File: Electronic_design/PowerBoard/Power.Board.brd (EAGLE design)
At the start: 100 x 80 mm, 33 parts, among them IC1 788TV, IC2 788TV

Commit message: ameliorations
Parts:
- U$1: value TROU_FIXATION -> (none)
- moved LED6 2.90 mm to (82.5, 6.22), turned to 270 degrees
- moved U$5 2.84 mm to (7.62, 74.9), turned to 0 degrees
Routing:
- net 12V: track 124.0 -> 78.3 mm
- net N$17: track 9.78 -> 9.02 mm
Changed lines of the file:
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@@
 <wire x1="0" y1="80" x2="0.381" y2="0" width="0" layer="20"/>
 <text x="5.08" y="2.54" size="1.778" layer="25" font="vector" rot="R90">LAAS_CNRS</text>
-<text x="15.24" y="73.66" size="1.778" layer="25" font="vector" rot="R180">GND</text>
+<text x="7.62" y="71.12" size="1.778" layer="25" font="vector" rot="R270">GND</text>
 <text x="88.9" y="66.04" size="1.778" layer="25" font="vector" rot="R270">GND</text>
 <text x="88.9" y="50.8" size="1.778" layer="25" font="vector">GND</text>
@@
 <text x="88.9" y="25.4" size="1.778" layer="25" font="vector">GND</text>
 <text x="93.98" y="2.54" size="1.778" layer="25" font="vector" rot="R180">GND</text>
-<text x="93.98" y="12.7" size="1.778" layer="25" font="vector" rot="R180">GND</text>
-<text x="10.16" y="63.5" size="1.778" layer="25" font="vector">12V</text>
+<text x="92.837" y="12.319" size="1.778" layer="25" font="vector" rot="R180">GND</text>
+<text x="16.51" y="71.12" size="1.778" layer="25" font="vector" rot="R270">12V</text>
 <text x="88.9" y="76.2" size="1.778" layer="25" font="vector" rot="R270">12V</text>
 <text x="88.9" y="55.88" size="1.778" layer="25" font="vector">12V</text>
@@
 <element name="MAST1" library="AUTO_FUSE" package="AUTO_FUSE" value="AUTO_FUSE" x="35.56" y="55.88"/>
 <element name="PAP1" library="AUTO_FUSE" package="AUTO_FUSE" value="AUTO_FUSE" x="35.56" y="43.18"/>
-<element name="U$5" library="PowerHeaders" package="3MM_HEADER_2" value="3MM_HEADER_2" x="5.08" y="73.66" rot="R270"/>
+<element name="U$5" library="PowerHeaders" package="3MM_HEADER_2" value="3MM_HEADER_2" x="7.62" y="74.93"/>
 <element name="0D2" library="AUTO_FUSE" package="AUTO_FUSE" value="AUTO_FUSE" x="58.42" y="68.58"/>
 <element name="MAST2" library="AUTO_FUSE" package="AUTO_FUSE" value="AUTO_FUSE" x="58.42" y="55.88"/>
@@
 <attribute name="SPICEPREFIX" value="R" x="78.74" y="7.62" size="1.778" layer="27" rot="R90" display="off"/>
 </element>
-<element name="LED6" library="eagle-ltspice" library_urn="urn:adsk.eagle:library:217" package="LED_LD260" package3d_urn="urn:adsk.eagle:package:13313/1" value="" x="85.217" y="5.08">
-<attribute name="SPICEMODEL" value="NONE" x="85.217" y="5.08" size="1.778" layer="27" display="off"/>
-<attribute name="SPICEPREFIX" value="D" x="85.217" y="5.08" size="1.778" layer="27" display="off"/>
-<attribute name="SPICETYPE" value="diode" x="85.217" y="5.08" size="1.778" layer="27" display="off"/>
+<element name="LED6" library="eagle-ltspice" library_urn="urn:adsk.eagle:library:217" package="LED_LD260" package3d_urn="urn:adsk.eagle:package:13313/1" value="" x="82.55" y="6.223" rot="R270">
+<attribute name="SPICEMODEL" value="NONE" x="82.55" y="6.223" size="1.778" layer="27" rot="R270" display="off"/>
+<attribute name="SPICEPREFIX" value="D" x="82.55" y="6.223" size="1.778" layer="27" rot="R270" display="off"/>
+<attribute name="SPICETYPE" value="diode" x="82.55" y="6.223" size="1.778" layer="27" rot="R270" display="off"/>
 </element>
 <element name="IC2" library="linear" library_urn="urn:adsk.eagle:library:262" package="TO220V" package3d_urn="urn:adsk.eagle:package:16417/1" value="788TV" x="58.42" y="7.62"/>
-<element name="U$1" library="Trous_fixation" package="TROUS_FIXATION" value="TROU_FIXATION" x="0" y="0"/>
+<element name="U$1" library="Trous_fixation" package="TROUS_FIXATION" value="" x="0" y="0"/>
 </elements>
 <signals>
@@
 <contactref element="RPI" pad="1A"/>
 <contactref element="FNU1" pad="P$2"/>
-<wire x1="22.86" y1="63.5" x2="5.08" y2="63.5" width="5" layer="16"/>
-<wire x1="22.86" y1="63.5" x2="24.13" y2="63.5" width="5" layer="16"/>
-<wire x1="24.13" y1="63.5" x2="28.45" y2="67.82" width="5" layer="16"/>
-<wire x1="28.45" y1="67.82" x2="28.45" y2="68.58" width="5" layer="16"/>
-<wire x1="28.45" y1="57.91" x2="28.45" y2="55.88" width="5" layer="16"/>
-<wire x1="28.45" y1="57.91" x2="22.86" y2="63.5" width="5" layer="16"/>
-<wire x1="28.45" y1="67.82" x2="28.45" y2="68.58" width="5" layer="1"/>
-<wire x1="22.86" y1="63.5" x2="24.13" y2="63.5" width="5" layer="1"/>
-<wire x1="24.13" y1="63.5" x2="28.45" y2="67.82" width="5" layer="1"/>
-<wire x1="28.45" y1="57.91" x2="28.45" y2="55.88" width="5" layer="1"/>
-<wire x1="28.45" y1="57.91" x2="22.86" y2="63.5" width="5" layer="1"/>
 <wire x1="28.45" y1="55.88" x2="28.45" y2="43.18" width="5" layer="1"/>
 <wire x1="28.45" y1="43.18" x2="28.45" y2="30.48" width="5" layer="1"/>
@@
 <wire x1="25.146" y1="15.24" x2="25.146" y2="5.334" width="5" layer="1"/>
 <wire x1="25.146" y1="5.334" x2="25.4" y2="5.08" width="5" layer="1"/>
-<wire x1="5.08" y1="63.5" x2="22.86" y2="63.5" width="5" layer="1"/>
+<wire x1="28.45" y1="68.58" x2="28.45" y2="55.88" width="5" layer="1"/>
+<wire x1="17.78" y1="74.93" x2="24.13" y2="68.58" width="6" layer="1"/>
+<wire x1="24.13" y1="68.58" x2="28.45" y2="68.58" width="6" layer="1"/>
 </signal>
 <signal name="N$2">
@@
 <contactref element="R6" pad="1"/>
 <contactref element="IC2" pad="3"/>
-<wire x1="60.96" y1="5.08" x2="68.58" y2="5.08" width="2.54" layer="16"/>
-<wire x1="68.58" y1="5.08" x2="71.12" y2="2.54" width="2.54" layer="16"/>
-<wire x1="71.12" y1="2.54" x2="78.74" y2="2.54" width="2.54" layer="16"/>
-<wire x1="78.74" y1="2.54" x2="88.9" y2="2.54" width="2.54" layer="16"/>
-<wire x1="88.9" y1="2.54" x2="91.44" y2="5.08" width="2.54" layer="16"/>
-<wire x1="91.44" y1="5.08" x2="96.52" y2="5.08" width="2.54" layer="16"/>
+<wire x1="60.96" y1="5.08" x2="67.31" y2="5.08" width="1.27" layer="16"/>
+<wire x1="67.31" y1="5.08" x2="69.85" y2="2.54" width="1.27" layer="16"/>
+<wire x1="69.85" y1="2.54" x2="78.74" y2="2.54" width="1.27" layer="16"/>
+<wire x1="78.74" y1="2.54" x2="88.9" y2="2.54" width="1.27" layer="16"/>
+<wire x1="88.9" y1="2.54" x2="91.44" y2="5.08" width="1.27" layer="16"/>
+<wire x1="91.44" y1="5.08" x2="96.52" y2="5.08" width="1.27" layer="16"/>
 </signal>
 <signal name="N$5">
@@
 <contactref element="R6" pad="2"/>
 <contactref element="LED6" pad="A"/>
-<wire x1="78.74" y1="12.7" x2="83.947" y2="7.493" width="1.27" layer="16"/>
-<wire x1="83.947" y1="7.493" x2="83.947" y2="5.08" width="1.27" layer="16"/>
+<wire x1="78.74" y1="12.7" x2="82.55" y2="12.7" width="1.27" layer="16"/>
+<wire x1="82.55" y1="12.7" x2="82.55" y2="7.493" width="1.27" layer="16"/>
 </signal>
 <signal name="N$18">

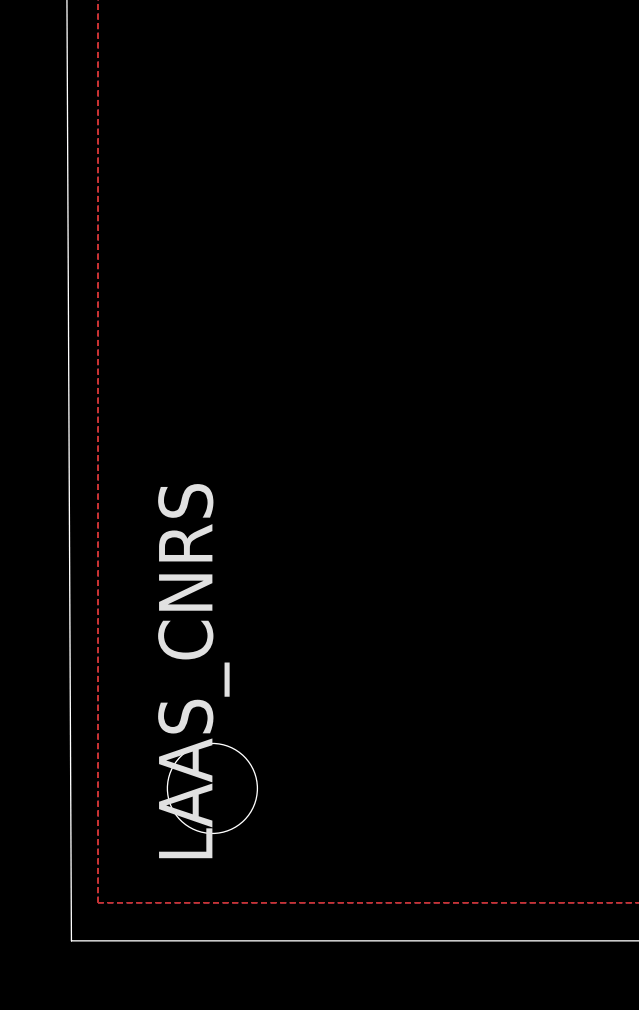
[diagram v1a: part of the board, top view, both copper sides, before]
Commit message: elargissement pistes
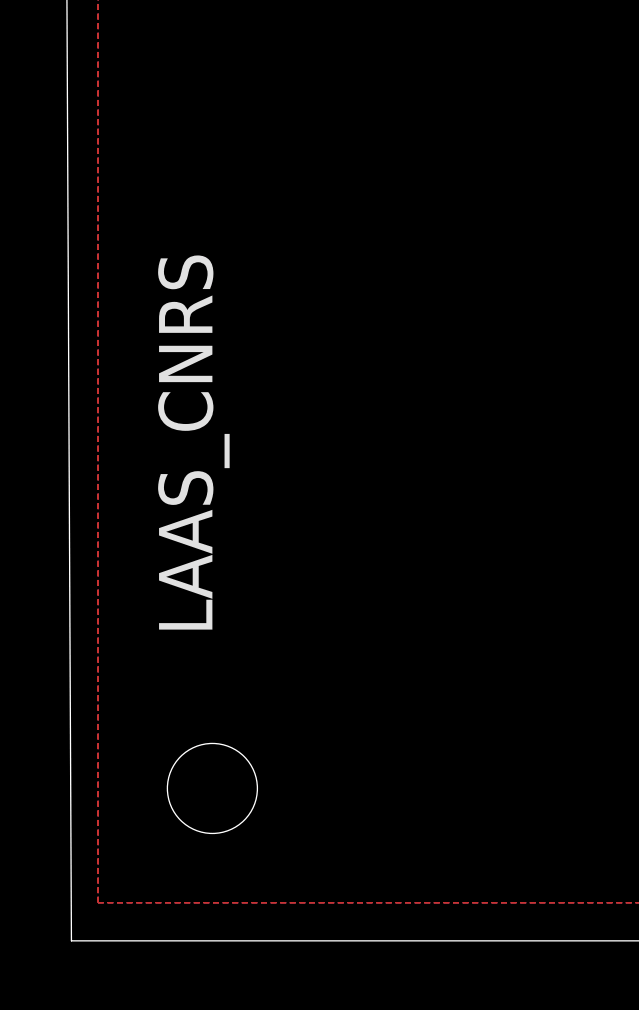
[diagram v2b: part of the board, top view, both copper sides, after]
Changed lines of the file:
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@@
 <wire x1="100" y1="80" x2="0" y2="80" width="0" layer="20"/>
 <wire x1="0" y1="80" x2="0.381" y2="0" width="0" layer="20"/>
-<text x="5.08" y="2.54" size="1.778" layer="25" font="vector" rot="R90">LAAS_CNRS</text>
+<text x="5.08" y="10.16" size="1.778" layer="25" font="vector" rot="R90">LAAS_CNRS</text>
 <text x="7.62" y="71.12" size="1.778" layer="25" font="vector" rot="R270">GND</text>
 <text x="88.9" y="66.04" size="1.778" layer="25" font="vector" rot="R270">GND</text>

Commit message: modif plan de masse
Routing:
- net 12V: track 78.3 -> 0.00 mm
- net N$6: track 36.9 -> 6.34 mm
- added copper zone on layer 1, net 12V
- added copper zone on layer 1, net N$6
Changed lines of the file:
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@@
 <contactref element="RPI" pad="1A"/>
 <contactref element="FNU1" pad="P$2"/>
-<wire x1="28.45" y1="55.88" x2="28.45" y2="43.18" width="5" layer="1"/>
-<wire x1="28.45" y1="43.18" x2="28.45" y2="30.48" width="5" layer="1"/>
-<wire x1="28.45" y1="30.48" x2="28.45" y2="25.91" width="5" layer="1"/>
-<wire x1="28.45" y1="25.91" x2="25.4" y2="22.86" width="5" layer="1"/>
-<wire x1="25.4" y1="22.86" x2="25.4" y2="15.494" width="5" layer="1"/>
-<wire x1="25.4" y1="15.494" x2="25.146" y2="15.24" width="5" layer="1"/>
-<wire x1="25.146" y1="15.24" x2="25.146" y2="5.334" width="5" layer="1"/>
-<wire x1="25.146" y1="5.334" x2="25.4" y2="5.08" width="5" layer="1"/>
-<wire x1="28.45" y1="68.58" x2="28.45" y2="55.88" width="5" layer="1"/>
-<wire x1="17.78" y1="74.93" x2="24.13" y2="68.58" width="6" layer="1"/>
-<wire x1="24.13" y1="68.58" x2="28.45" y2="68.58" width="6" layer="1"/>
+<polygon width="0.508" layer="1">
+<vertex x="1.27" y="78.74"/>
+<vertex x="35.56" y="78.74"/>
+<vertex x="35.60955" y="1.2763125"/>
+<vertex x="1.195678125" y="1.20198125"/>
+</polygon>
 </signal>
 <signal name="N$2">
@@
 <wire x1="65.53" y1="68.58" x2="68.58" y2="65.53" width="1.27" layer="16"/>
 <wire x1="68.58" y1="65.53" x2="68.58" y2="63.5" width="1.27" layer="16"/>
-<wire x1="65.53" y1="68.58" x2="68.58" y2="68.58" width="5" layer="1"/>
-<wire x1="68.58" y1="68.58" x2="73.66" y2="73.66" width="5" layer="1"/>
-<wire x1="73.66" y1="73.66" x2="93.98" y2="73.66" width="5" layer="1"/>
+<polygon width="0.508" layer="1">
+<vertex x="58.42" y="78.74"/>
+<vertex x="99.06" y="78.74"/>
+<vertex x="99.06" y="68.58"/>
+<vertex x="88.9" y="68.58"/>
+<vertex x="88.9" y="64.77"/>
+<vertex x="58.42" y="64.77"/>
+</polygon>
 </signal>
 <signal name="N$7">
@@
 <contactref element="MAST2" pad="P$4"/>
 <contactref element="R2" pad="1"/>
-<wire x1="65.53" y1="55.88" x2="76.2" y2="55.88" width="2.54" layer="16"/>
-<wire x1="76.2" y1="55.88" x2="95.25" y2="55.88" width="2.54" layer="16"/>
+<wire x1="65.53" y1="55.88" x2="76.2" y2="55.88" width="3" layer="16"/>
+<wire x1="76.2" y1="55.88" x2="95.25" y2="55.88" width="3" layer="16"/>
 </signal>
 <signal name="GND">
@@
 <contactref element="LED6" pad="K"/>
 <contactref element="IC2" pad="2"/>
-<polygon width="0.508" layer="1">
+<polygon width="0.508" layer="16">
 <vertex x="1.27" y="78.74"/>
 <vertex x="99.06" y="78.74"/>
@@
 </polygon>
 <polygon width="0.508" layer="1">
-<vertex x="1.27" y="78.74"/>
-<vertex x="99.06" y="78.74"/>
+<vertex x="36.83" y="78.74"/>
+<vertex x="57.15" y="78.74"/>
+<vertex x="57.15" y="63.5"/>
+<vertex x="90.17" y="63.5"/>
+<vertex x="90.17" y="67.31"/>
+<vertex x="99.06" y="67.31"/>
 <vertex x="99.06" y="1.27"/>
-<vertex x="1.27" y="1.27"/>
-</polygon>
-<polygon width="0.508" layer="16">
-<vertex x="1.27" y="78.74"/>
-<vertex x="99.06" y="78.74"/>
-<vertex x="99.06" y="1.27"/>
-<vertex x="1.27" y="1.27"/>
+<vertex x="36.83" y="1.27"/>
 </polygon>
 </signal>
@@
 <contactref element="PAP" pad="P$1"/>
 <contactref element="R3" pad="1"/>
-<wire x1="65.53" y1="43.18" x2="73.66" y2="43.18" width="2.54" layer="16"/>
-<wire x1="73.66" y1="43.18" x2="95.25" y2="43.18" width="2.54" layer="16"/>
+<wire x1="65.53" y1="43.18" x2="73.66" y2="43.18" width="3" layer="16"/>
+<wire x1="73.66" y1="43.18" x2="95.25" y2="43.18" width="3" layer="16"/>
 </signal>
 <signal name="N$8">

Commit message: ajout condensateurs
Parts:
- added C1, C2, C3: (no value), rcl:E7,5-18
- added C4: (no value), rcl:E5-13
- moved LED1 12.7 mm to (82.5, 76.2)
- moved R1 12.7 mm to (73.7, 76.2)
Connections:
- net 12V: now also C1.+, C2.+, C3.+
- net GND: now also C1.-, C2.-, C3.-, C4.-
- net N$6: now also C4.+
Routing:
- net N$6: track 6.34 -> 0.00 mm
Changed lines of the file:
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@@
 <wire x1="100" y1="80" x2="0" y2="80" width="0" layer="20"/>
 <wire x1="0" y1="80" x2="0.381" y2="0" width="0" layer="20"/>
-<text x="5.08" y="10.16" size="1.778" layer="25" font="vector" rot="R90">LAAS_CNRS</text>
+<text x="20.32" y="6.35" size="1.778" layer="25" font="vector" rot="R180">LAAS_CNRS</text>
 <text x="7.62" y="71.12" size="1.778" layer="25" font="vector" rot="R270">GND</text>
 <text x="88.9" y="66.04" size="1.778" layer="25" font="vector" rot="R270">GND</text>
@@
 <element name="FNU2" library="AUTO_FUSE" package="AUTO_FUSE" value="AUTO_FUSE" x="58.42" y="30.48"/>
 <element name="NOTUSE" library="PowerHeaders" package="GREEN_HEADER" value="GREEN_HEADER" x="95.25" y="27.94" rot="R270"/>
-<element name="LED1" library="eagle-ltspice" library_urn="urn:adsk.eagle:library:217" package="LED_LD260" package3d_urn="urn:adsk.eagle:package:13313/1" value="" x="82.55" y="63.5">
-<attribute name="SPICEMODEL" value="NONE" x="82.55" y="63.5" size="1.778" layer="27" display="off"/>
-<attribute name="SPICEPREFIX" value="D" x="82.55" y="63.5" size="1.778" layer="27" display="off"/>
-<attribute name="SPICETYPE" value="diode" x="82.55" y="63.5" size="1.778" layer="27" display="off"/>
-</element>
-<element name="R1" library="eagle-ltspice" library_urn="urn:adsk.eagle:library:217" package="0207/10" package3d_urn="urn:adsk.eagle:package:13275/1" value="" x="73.66" y="63.5">
-<attribute name="SPICEMODEL" value="NONE" x="73.66" y="63.5" size="1.778" layer="27" display="off"/>
-<attribute name="SPICEPREFIX" value="R" x="73.66" y="63.5" size="1.778" layer="27" display="off"/>
+<element name="LED1" library="eagle-ltspice" library_urn="urn:adsk.eagle:library:217" package="LED_LD260" package3d_urn="urn:adsk.eagle:package:13313/1" value="" x="82.55" y="76.2">
+<attribute name="SPICEMODEL" value="NONE" x="82.55" y="76.2" size="1.778" layer="27" display="off"/>
+<attribute name="SPICEPREFIX" value="D" x="82.55" y="76.2" size="1.778" layer="27" display="off"/>
+<attribute name="SPICETYPE" value="diode" x="82.55" y="76.2" size="1.778" layer="27" display="off"/>
+</element>
+<element name="R1" library="eagle-ltspice" library_urn="urn:adsk.eagle:library:217" package="0207/10" package3d_urn="urn:adsk.eagle:package:13275/1" value="" x="73.66" y="76.2">
+<attribute name="SPICEMODEL" value="NONE" x="73.66" y="76.2" size="1.778" layer="27" display="off"/>
+<attribute name="SPICEPREFIX" value="R" x="73.66" y="76.2" size="1.778" layer="27" display="off"/>
 </element>
 <element name="R2" library="eagle-ltspice" library_urn="urn:adsk.eagle:library:217" package="0207/10" package3d_urn="urn:adsk.eagle:package:13275/1" value="" x="76.2" y="50.8" rot="R270">
@@
 <element name="IC2" library="linear" library_urn="urn:adsk.eagle:library:262" package="TO220V" package3d_urn="urn:adsk.eagle:package:16417/1" value="788TV" x="58.42" y="7.62"/>
 <element name="U$1" library="Trous_fixation" package="TROUS_FIXATION" value="" x="0" y="0"/>
+<element name="C1" library="rcl" library_urn="urn:adsk.eagle:library:334" package="E7,5-18" package3d_urn="urn:adsk.eagle:package:23379/1" value="" x="13.97" y="57.15"/>
+<element name="C2" library="rcl" library_urn="urn:adsk.eagle:library:334" package="E7,5-18" package3d_urn="urn:adsk.eagle:package:23379/1" value="" x="13.97" y="39.37"/>
+<element name="C3" library="rcl" library_urn="urn:adsk.eagle:library:334" package="E7,5-18" package3d_urn="urn:adsk.eagle:package:23379/1" value="" x="13.97" y="21.59"/>
+<element name="C4" library="rcl" library_urn="urn:adsk.eagle:library:334" package="E5-13" package3d_urn="urn:adsk.eagle:package:23375/1" value="" x="76.2" y="64.77" rot="R270"/>
 </elements>
 <signals>
@@
 <vertex x="1.195678125" y="1.20198125"/>
 </polygon>
+<contactref element="C1" pad="+"/>
+<contactref element="C2" pad="+"/>
+<contactref element="C3" pad="+"/>
 </signal>
 <signal name="N$2">
@@
 <contactref element="OD" pad="P$1"/>
 <contactref element="R1" pad="1"/>
-<wire x1="65.53" y1="68.58" x2="68.58" y2="65.53" width="1.27" layer="16"/>
-<wire x1="68.58" y1="65.53" x2="68.58" y2="63.5" width="1.27" layer="16"/>
 <polygon width="0.508" layer="1">
 <vertex x="58.42" y="78.74"/>
@@
 <vertex x="58.42" y="64.77"/>
 </polygon>
+<contactref element="C4" pad="+"/>
 </signal>
 <signal name="N$7">
@@
 <vertex x="36.83" y="1.27"/>
 </polygon>
+<contactref element="C1" pad="-"/>
+<contactref element="C2" pad="-"/>
+<contactref element="C3" pad="-"/>
+<contactref element="C4" pad="-"/>
 </signal>
 <signal name="N$1">
@@
 <contactref element="LED1" pad="A"/>
 <contactref element="R1" pad="2"/>
-<wire x1="78.74" y1="63.5" x2="81.28" y2="63.5" width="1.27" layer="16"/>
+<wire x1="78.74" y1="76.2" x2="81.28" y2="76.2" width="1.27" layer="16"/>
 </signal>
 <signal name="N$13">

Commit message: modif sens connecteurs puissance
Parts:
- moved U$5 10.2 mm to (17.8, 74.9), turned to 180 degrees
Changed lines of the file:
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@@
 <wire x1="0" y1="80" x2="0.381" y2="0" width="0" layer="20"/>
 <text x="20.32" y="6.35" size="1.778" layer="25" font="vector" rot="R180">LAAS_CNRS</text>
-<text x="7.62" y="71.12" size="1.778" layer="25" font="vector" rot="R270">GND</text>
+<text x="16.51" y="71.12" size="1.778" layer="25" font="vector" rot="R270">GND</text>
 <text x="88.9" y="66.04" size="1.778" layer="25" font="vector" rot="R270">GND</text>
 <text x="88.9" y="50.8" size="1.778" layer="25" font="vector">GND</text>
@@
 <text x="93.98" y="2.54" size="1.778" layer="25" font="vector" rot="R180">GND</text>
 <text x="92.837" y="12.319" size="1.778" layer="25" font="vector" rot="R180">GND</text>
-<text x="16.51" y="71.12" size="1.778" layer="25" font="vector" rot="R270">12V</text>
+<text x="7.62" y="71.12" size="1.778" layer="25" font="vector" rot="R270">12V</text>
 <text x="88.9" y="76.2" size="1.778" layer="25" font="vector" rot="R270">12V</text>
 <text x="88.9" y="55.88" size="1.778" layer="25" font="vector">12V</text>
@@
 <element name="MAST1" library="AUTO_FUSE" package="AUTO_FUSE" value="AUTO_FUSE" x="35.56" y="55.88"/>
 <element name="PAP1" library="AUTO_FUSE" package="AUTO_FUSE" value="AUTO_FUSE" x="35.56" y="43.18"/>
-<element name="U$5" library="PowerHeaders" package="3MM_HEADER_2" value="3MM_HEADER_2" x="7.62" y="74.93"/>
+<element name="U$5" library="PowerHeaders" package="3MM_HEADER_2" value="3MM_HEADER_2" x="17.78" y="74.93" smashed="yes" rot="R180"/>
 <element name="0D2" library="AUTO_FUSE" package="AUTO_FUSE" value="AUTO_FUSE" x="58.42" y="68.58"/>
 <element name="MAST2" library="AUTO_FUSE" package="AUTO_FUSE" value="AUTO_FUSE" x="58.42" y="55.88"/>
